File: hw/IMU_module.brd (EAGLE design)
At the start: 25 x 45 mm, 23 parts, among them J1 GROVE-4P-2.0-3470130P1, J2 GROVE-4P-2.0-3470130P1

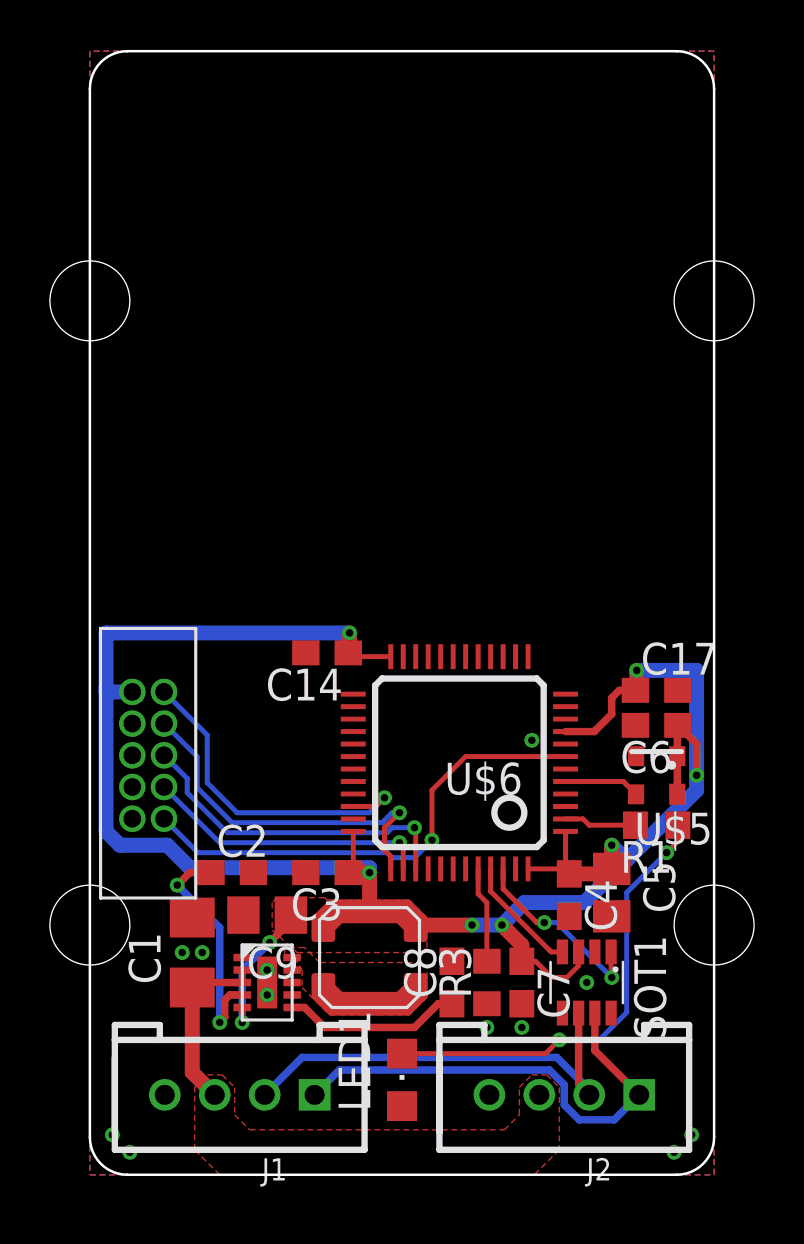
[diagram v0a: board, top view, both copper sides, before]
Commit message: added MEMS datasheets to doc foder
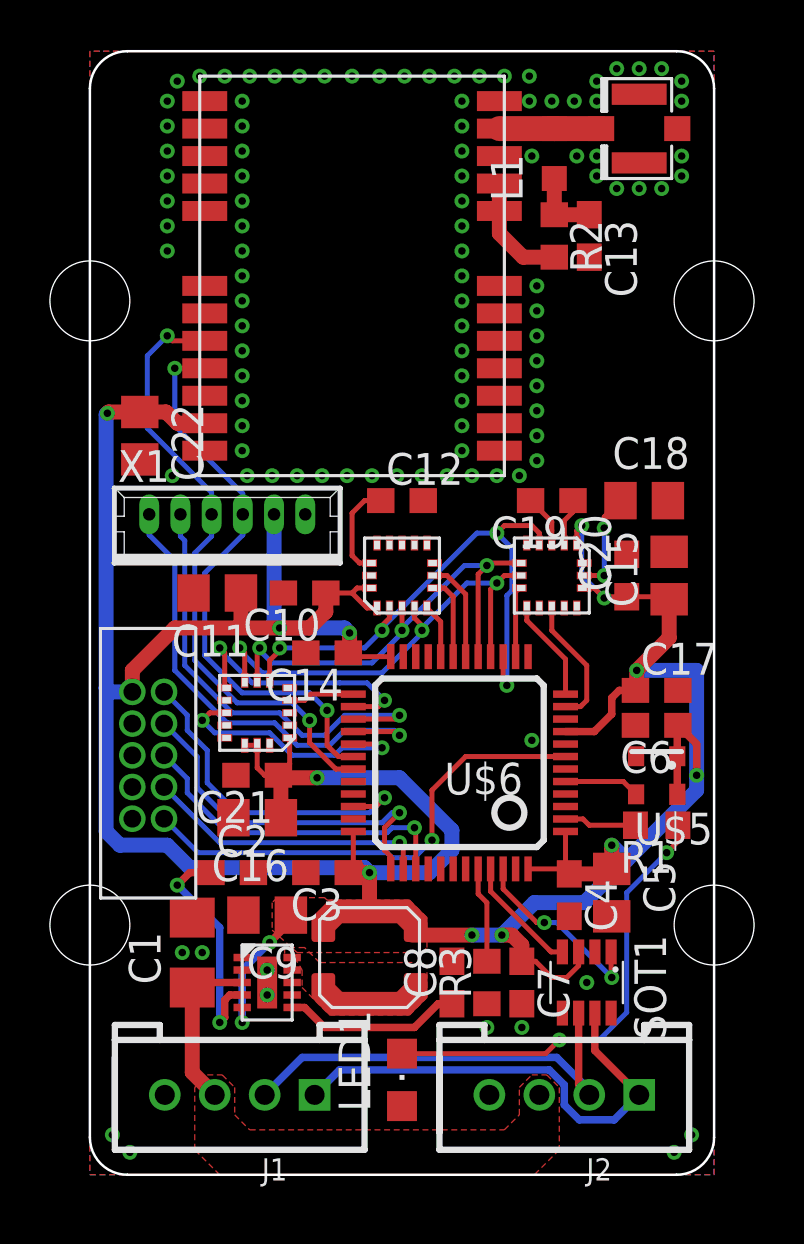
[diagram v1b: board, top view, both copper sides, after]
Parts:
- added C10, C13, C20, C21: 100n, rcl:C0603
- added C11, C15, C16: 10u, rcl:C0805
- added C12: 10n, rcl:C0603
- added C18, C22: 4.7u, rcl:C0805
- added C19: 220n, rcl:C0603
- added L1: (no value), rcl:L2012C
- added R2: 10, rcl:R0603
- added U$10: NEO-6, u-blox:NEO
- added U$11: U.FL, SparkFun:U.FL
- added U$7: L3GD20H, st:LGA16L
- added U$8: LSM303D, st:LGA16L
- added U$9: LPS331AP, st:LGA16L
- added X1: 53047-06, con-molex:53047-06
- U$6: value STM32F103CX -> STM32F103CXTX
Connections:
- new net AM_CS: U$6.14, U$8.P$8
- new net AM_INT1: U$6.11, U$8.P$11
- new net AM_INT2: U$6.12, U$8.P$9
- new net BAR_CS: U$6.25, U$9.P$4
- new net BAR_INT1: U$6.29, U$9.P$11
- new net BAR_INT2: U$6.26, U$9.P$9
- new net GPS_AUX1: U$6.27, X1.5
- new net GPS_AUX2: U$6.28, X1.6
- new net GPS_RX: U$10.P$21, U$6.30, X1.3
- new net GPS_TX: U$10.P$20, U$6.31, X1.4
- new net GYRO_CS: U$6.20, U$7.P$5
- new net GYRO_INT1: U$6.18, U$7.P$7
- new net GYRO_INT2: U$6.19, U$7.P$6
- new net MISO: U$6.16, U$7.P$4, U$8.P$7, U$9.P$8
- new net MOSI: U$6.17, U$7.P$3, U$8.P$6, U$9.P$7
- new net N$10: L1.2, U$10.P$11, U$11.P$3
- new net N$11: C13.1, L1.1, R2.1
- new net N$12: R2.2, U$10.P$8, U$10.P$9
- new net N$3: C12.1, U$7.P$14
- new net N$5: C18.1, U$8.P$15
- new net N$6: C19.1, U$8.P$2
- new net N$9: C19.2, U$8.P$3
- new net SCK: U$6.15, U$7.P$2, U$8.P$4, U$9.P$6
- net +3V3: now also C10.1, C11.1, C15.1, C16.1, C20.1, C21.1, C22.1, U$10.P$23, U$7.P$1, U$7.P$16, U$8.P$1, U$8.P$14, U$9.P$1, U$9.P$14, U$9.P$15, X1.2
- net GND: now also C10.2, C11.2, C12.2, C13.2, C15.2, C16.2, C18.2, C20.2, C21.2, C22.2, U$10.P$10, U$10.P$12, U$10.P$13, U$10.P$22, U$10.P$24, U$10.P$7, U$7.P$10, U$7.P$11, U$7.P$12, U$7.P$13, U$7.P$15, U$7.P$8, U$7.P$9, U$8.P$10, U$8.P$12, U$8.P$13, U$8.P$16, U$8.P$5, U$9.P$10, U$9.P$12, U$9.P$13, U$9.P$16, U$9.P$5, X1.1
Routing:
- net +3V3: track 86.0 -> 140.7 mm, vias 9 -> 14
- net GPS_TX: track 0.00 -> 24.9 mm, vias 0 -> 2
- net SCK: track 0.00 -> 23.1 mm, vias 0 -> 4
- net GPS_RX: track 0.00 -> 22.9 mm, vias 0 -> 2
- net GPS_AUX2: track 0.00 -> 19.2 mm, vias 0 -> 1
- net MISO: track 0.00 -> 18.9 mm, vias 0 -> 3
- net MOSI: track 0.00 -> 18.5 mm, vias 0 -> 3
- net GPS_AUX1: track 0.00 -> 18.1 mm, vias 0 -> 1
- net BAR_INT2: track 0.00 -> 10.6 mm, vias 0 -> 2
- net BAR_INT1: track 0.00 -> 10.1 mm, vias 0 -> 2
- net AM_INT1: track 0.00 -> 5.23 mm
- net N$12: track 0.00 -> 4.59 mm
- net N$10: track 0.00 -> 4.18 mm
- net AM_INT2: track 0.00 -> 4.09 mm
- net N$5: track 0.00 -> 4.07 mm, vias 0 -> 2
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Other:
- board text added: "Y"
- board text added: "Z"
- board text added: "x"

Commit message: added TIMEPULSE and INT0 signals
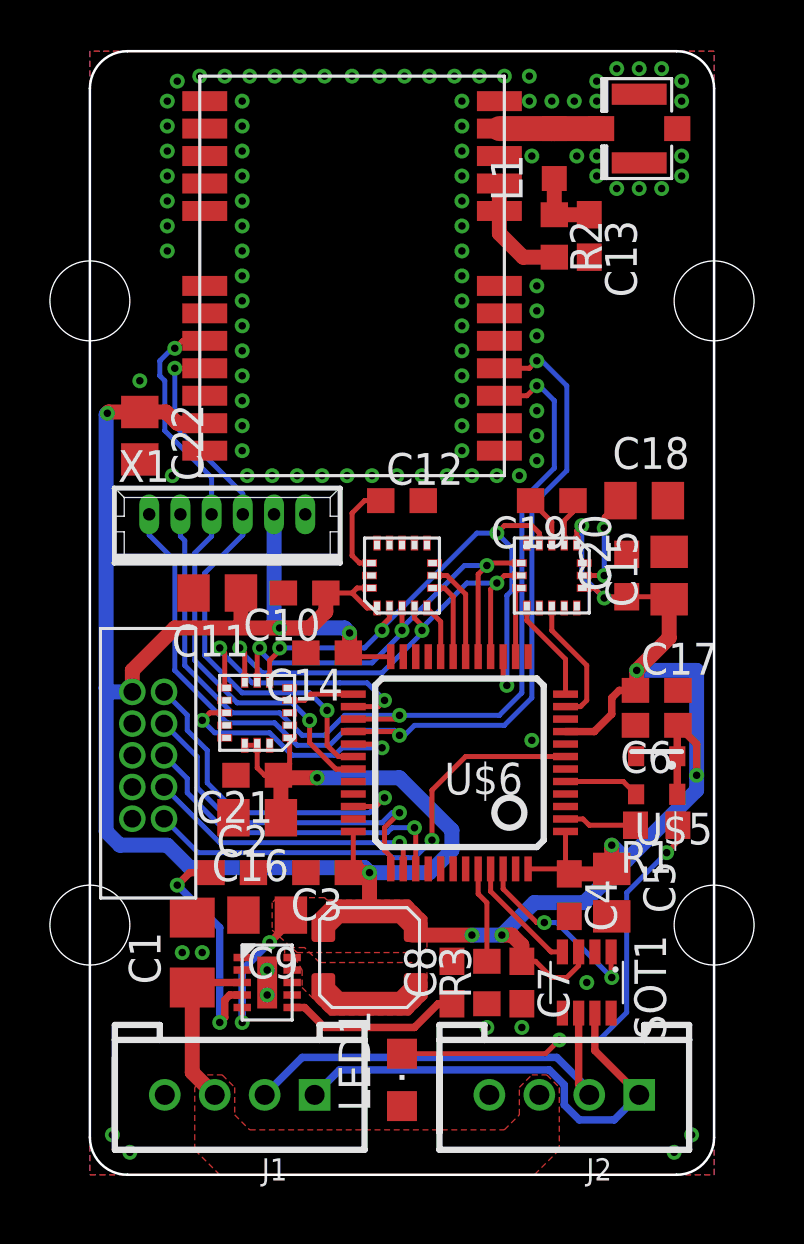
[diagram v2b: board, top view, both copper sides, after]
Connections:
- net GPS_AUX1: now also U$10.P$3
- net GPS_AUX2: now also U$10.P$4
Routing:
- net GPS_AUX2: track 19.2 -> 41.4 mm, vias 1 -> 2
- net GPS_AUX1: track 18.1 -> 38.3 mm, vias 1 -> 2
- net GPS_TX: track 24.9 -> 23.9 mm
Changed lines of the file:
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@@
 <via x="17.9" y="34.6" extent="1-16" drill="0.3"/>
 <via x="17.9" y="33.6" extent="1-16" drill="0.3"/>
-<via x="17.9" y="32.6" extent="1-16" drill="0.3"/>
-<via x="17.9" y="31.6" extent="1-16" drill="0.3"/>
 <via x="17.9" y="30.6" extent="1-16" drill="0.3"/>
 <via x="17.9" y="29.6" extent="1-16" drill="0.3"/>
@@
 <via x="14.9" y="29" extent="1-16" drill="0.3"/>
 <via x="3.3" y="28" extent="1-16" drill="0.3"/>
+<via x="2" y="31.8" extent="1-16" drill="0.3"/>
 </signal>
 <signal name="VIN">
@@
 <signal name="GPS_TX">
 <contactref element="U$10" pad="P$20"/>
-<via x="3.1" y="33.6" extent="1-16" drill="0.3"/>
+<via x="3.4" y="33.1" extent="1-16" drill="0.3"/>
 <contactref element="X1" pad="4"/>
 <via x="8.8" y="18.2" extent="1-16" drill="0.3"/>
@@
 <wire x1="4.2" y1="20.6" x2="5.9" y2="18.9" width="0.2" layer="16"/>
 <wire x1="5.9" y1="18.9" x2="8.1" y2="18.9" width="0.2" layer="16"/>
-<wire x1="4.6" y1="33.4" x2="3.3" y2="33.4" width="0.2" layer="1"/>
-<wire x1="3.3" y1="33.4" x2="3.1" y2="33.6" width="0.2" layer="1"/>
-<wire x1="3.1" y1="33.6" x2="2.3" y2="32.8" width="0.2" layer="16"/>
-<wire x1="2.3" y1="32.8" x2="2.3" y2="29.9" width="0.2" layer="16"/>
-<wire x1="2.3" y1="29.9" x2="4.875" y2="27.325" width="0.2" layer="16"/>
 <wire x1="4.875" y1="27.325" x2="4.875" y2="26.45" width="0.2" layer="16"/>
+<wire x1="4.875" y1="27.325" x2="4.875" y2="27.925" width="0.2" layer="16"/>
+<wire x1="4.875" y1="27.925" x2="3" y2="29.8" width="0.2" layer="16"/>
+<wire x1="3" y1="29.8" x2="3" y2="31.8" width="0.2" layer="16"/>
+<wire x1="3" y1="31.8" x2="2.8" y2="32" width="0.2" layer="16"/>
+<wire x1="2.8" y1="32" x2="2.8" y2="32.6" width="0.2" layer="16"/>
+<wire x1="2.8" y1="32.6" x2="3.3" y2="33.1" width="0.2" layer="16"/>
+<wire x1="3.3" y1="33.1" x2="3.4" y2="33.1" width="0.2" layer="16"/>
+<wire x1="4.6" y1="33.4" x2="3.7" y2="33.4" width="0.2" layer="1"/>
+<wire x1="3.7" y1="33.4" x2="3.4" y2="33.1" width="0.2" layer="1"/>
 </signal>
 <signal name="GPS_AUX1">
@@
 <wire x1="10.55" y1="18.25" x2="12.25" y2="18.25" width="0.2" layer="1"/>
 <wire x1="12.25" y1="18.25" x2="12.4" y2="18.4" width="0.2" layer="1"/>
+<contactref element="U$10" pad="P$3"/>
+<wire x1="16.4" y1="31.2" x2="17.5" y2="31.2" width="0.2" layer="1"/>
+<wire x1="17.5" y1="31.2" x2="17.9" y2="31.6" width="0.2" layer="1"/>
+<via x="17.9" y="31.6" extent="1-16" drill="0.3"/>
+<wire x1="17.9" y1="31.6" x2="18" y2="31.6" width="0.2" layer="16"/>
+<wire x1="18" y1="31.6" x2="18.6" y2="31" width="0.2" layer="16"/>
+<wire x1="18.6" y1="31" x2="18.6" y2="28.3" width="0.2" layer="16"/>
+<wire x1="18.6" y1="28.3" x2="17.3" y2="27" width="0.2" layer="16"/>
+<wire x1="17.3" y1="27" x2="17.3" y2="19.3" width="0.2" layer="16"/>
+<wire x1="17.3" y1="19.3" x2="16.4" y2="18.4" width="0.2" layer="16"/>
+<wire x1="16.4" y1="18.4" x2="12.4" y2="18.4" width="0.2" layer="16"/>
 </signal>
 <signal name="GPS_AUX2">
@@
 <wire x1="10.2" y1="17.8" x2="9.6" y2="17.2" width="0.2" layer="16"/>
 <wire x1="9.6" y1="17.2" x2="8.3" y2="17.2" width="0.2" layer="16"/>
+<contactref element="U$10" pad="P$4"/>
+<wire x1="16.4" y1="32.3" x2="17.6" y2="32.3" width="0.2" layer="1"/>
+<wire x1="17.6" y1="32.3" x2="17.9" y2="32.6" width="0.2" layer="1"/>
+<via x="17.9" y="32.6" extent="1-16" drill="0.3"/>
+<wire x1="17.9" y1="32.6" x2="18.1" y2="32.6" width="0.2" layer="16"/>
+<wire x1="18.1" y1="32.6" x2="19.1" y2="31.6" width="0.2" layer="16"/>
+<wire x1="19.1" y1="31.6" x2="19.1" y2="28.2" width="0.2" layer="16"/>
+<wire x1="19.1" y1="28.2" x2="17.7" y2="26.8" width="0.2" layer="16"/>
+<wire x1="17.7" y1="26.8" x2="17.7" y2="19.1" width="0.2" layer="16"/>
+<wire x1="17.7" y1="19.1" x2="16.6" y2="18" width="0.2" layer="16"/>
+<wire x1="16.6" y1="18" x2="13" y2="18" width="0.2" layer="16"/>
+<wire x1="12.4" y1="17.6" x2="12.6" y2="17.6" width="0.2" layer="16"/>
+<wire x1="12.6" y1="17.6" x2="13" y2="18" width="0.2" layer="16"/>
 </signal>
 <signal name="N$3">

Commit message: updated GPS connector to have Vcc on pin 1
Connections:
- net +3V3: now also X1.1; no longer X1.2
- net GND: now also X1.2; no longer X1.1
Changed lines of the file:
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@@
 <grid distance="0.5" unitdist="mm" unit="mm" style="dots" multiple="1" display="yes" altdistance="0.1" altunitdist="mm" altunit="mm"/>
 <layers>
-<layer number="1" name="Top" color="4" fill="1" visible="yes" active="yes"/>
-<layer number="16" name="Bottom" color="1" fill="1" visible="no" active="yes"/>
+<layer number="1" name="Top" color="4" fill="1" visible="no" active="yes"/>
+<layer number="16" name="Bottom" color="1" fill="1" visible="yes" active="yes"/>
 <layer number="17" name="Pads" color="2" fill="1" visible="yes" active="yes"/>
 <layer number="18" name="Vias" color="2" fill="1" visible="yes" active="yes"/>
 <layer number="19" name="Unrouted" color="6" fill="1" visible="yes" active="yes"/>
 <layer number="20" name="Dimension" color="15" fill="1" visible="yes" active="yes"/>
-<layer number="21" name="tPlace" color="7" fill="1" visible="yes" active="yes"/>
-<layer number="22" name="bPlace" color="7" fill="1" visible="no" active="yes"/>
-<layer number="23" name="tOrigins" color="15" fill="1" visible="yes" active="yes"/>
-<layer number="24" name="bOrigins" color="15" fill="1" visible="no" active="yes"/>
+<layer number="21" name="tPlace" color="7" fill="1" visible="no" active="yes"/>
+<layer number="22" name="bPlace" color="7" fill="1" visible="yes" active="yes"/>
+<layer number="23" name="tOrigins" color="15" fill="1" visible="no" active="yes"/>
+<layer number="24" name="bOrigins" color="15" fill="1" visible="yes" active="yes"/>
 <layer number="25" name="tNames" color="7" fill="1" visible="no" active="yes"/>
 <layer number="26" name="bNames" color="7" fill="1" visible="no" active="yes"/>
@@
 <layer number="37" name="tTest" color="7" fill="1" visible="no" active="yes"/>
 <layer number="38" name="bTest" color="7" fill="1" visible="no" active="yes"/>
-<layer number="39" name="tKeepout" color="4" fill="11" visible="yes" active="yes"/>
-<layer number="40" name="bKeepout" color="1" fill="11" visible="no" active="yes"/>
-<layer number="41" name="tRestrict" color="4" fill="10" visible="yes" active="yes"/>
-<layer number="42" name="bRestrict" color="1" fill="10" visible="no" active="yes"/>
+<layer number="39" name="tKeepout" color="4" fill="11" visible="no" active="yes"/>
+<layer number="40" name="bKeepout" color="1" fill="11" visible="yes" active="yes"/>
+<layer number="41" name="tRestrict" color="4" fill="10" visible="no" active="yes"/>
+<layer number="42" name="bRestrict" color="1" fill="10" visible="yes" active="yes"/>
 <layer number="43" name="vRestrict" color="2" fill="10" visible="no" active="yes"/>
 <layer number="44" name="Drills" color="7" fill="1" visible="no" active="yes"/>
@@
 <layer number="46" name="Milling" color="3" fill="1" visible="yes" active="yes"/>
 <layer number="47" name="Measures" color="7" fill="1" visible="no" active="yes"/>
-<layer number="48" name="Document" color="7" fill="1" visible="yes" active="yes"/>
+<layer number="48" name="Document" color="7" fill="1" visible="no" active="yes"/>
 <layer number="49" name="Reference" color="7" fill="1" visible="no" active="yes"/>
 <layer number="50" name="dxf" color="7" fill="1" visible="no" active="no"/>
-<layer number="51" name="tDocu" color="7" fill="1" visible="yes" active="yes"/>
-<layer number="52" name="bDocu" color="7" fill="1" visible="no" active="yes"/>
+<layer number="51" name="tDocu" color="7" fill="1" visible="no" active="yes"/>
+<layer number="52" name="bDocu" color="7" fill="1" visible="yes" active="yes"/>
 <layer number="53" name="tGND_GNDA" color="7" fill="1" visible="no" active="no"/>
 <layer number="54" name="bGND_GNDA" color="7" fill="1" visible="no" active="no"/>
@@
 <contactref element="C16" pad="2"/>
 <contactref element="C21" pad="2"/>
-<contactref element="X1" pad="1"/>
 <contactref element="C12" pad="2"/>
 <contactref element="U$7" pad="P$12"/>
@@
 <via x="3.3" y="28" extent="1-16" drill="0.3"/>
 <via x="2" y="31.8" extent="1-16" drill="0.3"/>
+<contactref element="X1" pad="2"/>
 </signal>
 <signal name="VIN">
@@
 <contactref element="C15" pad="1"/>
 <contactref element="C20" pad="1"/>
-<contactref element="X1" pad="2"/>
 <contactref element="C11" pad="1"/>
 <contactref element="C10" pad="1"/>
@@
 <wire x1="5.9" y1="21.9" x2="3.4" y2="21.9" width="0.6" layer="1"/>
 <wire x1="3.4" y1="21.9" x2="1.7" y2="20.2" width="0.6" layer="1"/>
-<wire x1="7.375" y1="26.45" x2="7.375" y2="22.125" width="0.6" layer="16"/>
-<wire x1="7.375" y1="22.125" x2="7.6" y2="21.9" width="0.6" layer="16"/>
 <wire x1="6.05" y1="23.3" x2="6.05" y2="22.05" width="0.6" layer="1"/>
 <wire x1="6.05" y1="22.05" x2="5.9" y2="21.9" width="0.6" layer="1"/>
@@
 <wire x1="0.81" y1="19.34" x2="0.65" y2="19.5" width="0.6" layer="16"/>
 <wire x1="1.7" y1="20.2" x2="1.7" y2="19.34" width="0.6" layer="1"/>
+<contactref element="X1" pad="1"/>
+<wire x1="8.625" y1="26.45" x2="8.6" y2="26.425" width="0.6" layer="16"/>
+<wire x1="8.6" y1="26.425" x2="8.6" y2="25.7" width="0.6" layer="16"/>
+<wire x1="8.6" y1="25.7" x2="7.6" y2="24.7" width="0.6" layer="16"/>
+<wire x1="7.6" y1="24.7" x2="7.6" y2="21.9" width="0.6" layer="16"/>
 </signal>
 <signal name="JTMS">
